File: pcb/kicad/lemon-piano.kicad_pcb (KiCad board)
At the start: 2 copper layers, 100 x 30 mm, 44 parts, among them J1 5V_IN, J2 LEMON_KEYS, SW1 SENS+, SW2 SENS-, U1 Nano_socket_A, U2 Nano_socket_B

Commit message: fix(pcb): v0.2.0 — real Nano orientation (erratum ADR-015) + full render suite
The photo-overlay verification caught v0.1.0's socket maps being
180°-rotated (TX1/VIN are at the ICSP end on real Nanos, D12/D13 at the
mini-USB end — verified on the official 2008 V2.2 board photo and
clones). v0.1.0 only worked inserted USB-east, where the buzzer blocks
the plug; its release folder is renamed v0.1.0-ERRATUM-do-not-fab.

v0.2.0 keeps the mechanics (USB corridor west) and fixes the maps:
keys header SOUTH (1..7 G under A0-A6), LED bar NORTH ascending
east→west, pull-ups with their pins; ground truth, schematic, netlist
and every gate re-derived — DRC 0/0/0, ERC 0/0, verify_placement/
holes/geometry PASS, fab zip under pcb/releases/v0.2.0/.

Render suite via the pcb-designer service v0.3.0 (3D models installed):
bare / dim / realistic / realistic-dim per side + photo overlay with a
real Nano image (Wikimedia Commons File:Arduino Nano.jpg, CC BY 2.0,
provenance in pcb/overlays/modules.yaml). post_route self-healing
upgrades (connectivity-based island bridging, split-net repair, exact
clearance geometry, IsOnLayer fix) in ADR-018.

Co-Authored-By: Claude Fable 5 <noreply@anthropic.com>
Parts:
- moved D3 49.6 mm to (145.3, 101.7), turned to -90 degrees
- moved D12 48.9 mm to (103.9, 101.7), turned to -90 degrees
- moved R8 48.2 mm to (147.6, 103.0)
- moved R17 47.5 mm to (106.2, 103.0)
- moved D4 42.1 mm to (140.7, 101.7), turned to -90 degrees
- moved D11 41.5 mm to (108.5, 101.7), turned to -90 degrees
- moved R9 40.5 mm to (143.0, 103.0)
- moved R16 39.9 mm to (110.8, 103.0)
- moved D5 35.5 mm to (136.1, 101.7), turned to -90 degrees
- moved D10 34.9 mm to (113.1, 101.7), turned to -90 degrees
- moved R10 33.6 mm to (138.4, 103.0)
- moved R15 33.0 mm to (115.4, 103.0)
- moved D6 30.2 mm to (131.5, 101.7), turned to -90 degrees
- moved D9 29.8 mm to (117.7, 101.7), turned to -90 degrees
- moved R11 27.9 mm to (133.8, 103.0)
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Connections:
- J2 pad 1: /GND -> /KEY1
- J2 pad 2: /KEY7 -> /KEY2
- J2 pad 3: /KEY6 -> /KEY3
- J2 pad 4: /KEY5 -> /KEY4
- J2 pad 5: /KEY4 -> /KEY5
- J2 pad 6: /KEY3 -> /KEY6
- J2 pad 7: /KEY2 -> /KEY7
- J2 pad 8: /KEY1 -> /GND
- R1 pad 1: /+5V -> /KEY1
- R1 pad 2: /KEY1 -> /+5V
- R18 pad 1: /+5V -> /SENS_MINUS
- R18 pad 2: /SENS_MINUS -> /+5V
- R2 pad 1: /+5V -> /KEY2
- R2 pad 2: /KEY2 -> /+5V
- R3 pad 1: /+5V -> /KEY3
- R3 pad 2: /KEY3 -> /+5V
- R4 pad 1: /+5V -> /KEY4
- R4 pad 2: /KEY4 -> /+5V
- R5 pad 1: /+5V -> /KEY5
- R5 pad 2: /KEY5 -> /+5V
- R6 pad 1: /+5V -> /KEY6
- R6 pad 2: /KEY6 -> /+5V
- R7 pad 1: /+5V -> /KEY7
- R7 pad 2: /KEY7 -> /+5V
- U1 pad 1: (no net) -> /BUZZER
- U1 pad 10: /LED6 -> /KEY7
- U1 pad 11: /LED7 -> /SENS_MINUS
- U1 pad 12: /LED8 -> /+5V
- U1 pad 13: /LED9 -> (no net)
- U1 pad 14: /LED10 -> /GND
- U1 pad 15: /SENS_PLUS -> (no net)
- U1 pad 4: /GND -> /KEY1
- U1 pad 5: /LED1 -> /KEY2
- U1 pad 6: /LED2 -> /KEY3
- U1 pad 7: /LED3 -> /KEY4
- U1 pad 8: /LED4 -> /KEY5
- U1 pad 9: /LED5 -> /KEY6
- U2 pad 1: /BUZZER -> (no net)
- U2 pad 10: /KEY7 -> /LED6
- U2 pad 11: /SENS_MINUS -> /LED7
- U2 pad 12: /+5V -> /LED8
- U2 pad 13: (no net) -> /LED9
- U2 pad 14: /GND -> /LED10
- U2 pad 15: (no net) -> /SENS_PLUS
- U2 pad 4: /KEY1 -> /GND
- U2 pad 5: /KEY2 -> /LED1
- U2 pad 6: /KEY3 -> /LED2
- U2 pad 7: /KEY4 -> /LED3
- U2 pad 8: /KEY5 -> /LED4
- U2 pad 9: /KEY6 -> /LED5
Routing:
- net /SENS_PLUS: track 17.0 -> 58.9 mm
- net /BUZZER: track 10.5 -> 47.5 mm, vias 0 -> 1
- net /SENS_MINUS: track 61.5 -> 40.6 mm, vias 1 -> 0
- net /GND: track 0.00 -> 14.8 mm, vias 0 -> 1
- net /LED3: track 7.84 -> 14.8 mm
- net /+5V: track 80.0 -> 86.0 mm
- net /LED1: track 12.0 -> 17.2 mm
- net /LED4: track 5.78 -> 11.0 mm
- net /LED2: track 9.90 -> 15.2 mm
- net /LED10: track 9.18 -> 4.28 mm
- net /LED5: track 4.14 -> 8.98 mm
- net /LED9: track 7.12 -> 3.43 mm
- net /LED6: track 3.29 -> 6.92 mm
- net /LED7_K: track 3.93 -> 2.43 mm
- net /LED1_K: track 3.93 -> 2.43 mm
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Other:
- board text added: "v0.2.0"
- board text removed: "v0.1.0"

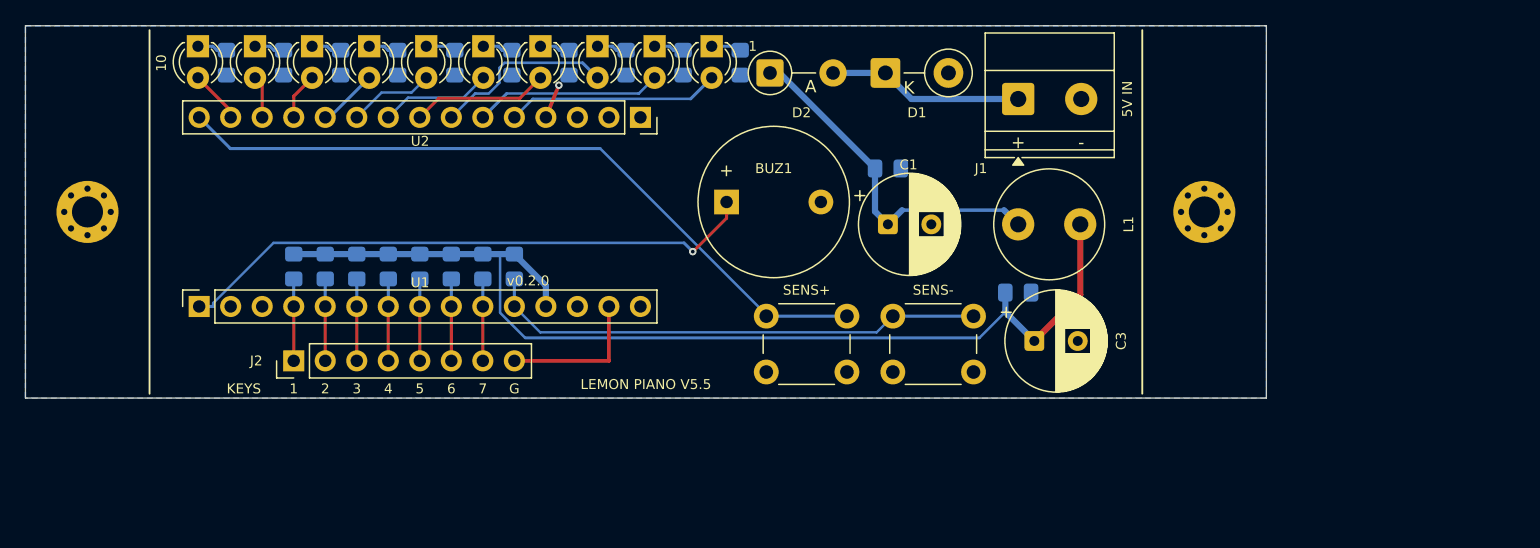
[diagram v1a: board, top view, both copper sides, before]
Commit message: feat(pcb): v0.2.1 — pin legends + full component labels + render suite naming
- 'pcb vX.Y.Z' version silk (front + back); MT1-style per-pin legends
  on both Nano socket rows; every component ref visible on its layer
  (bottom passives on B.SilkS; LED refs on the back — no front room at
  4.6 mm pitch). ADR-019.
- Render suite per version: renders/<ver>-{normal,dim,realistic,overlay}
  -{top,bottom}.png — realistic-dim dropped, overlay composites moved
  into renders/, overlays/ keeps only module photos + modules.yaml.
  v0.2.0 artefacts renamed/cleaned to the same scheme.
- Full gated pipeline re-run: DRC 0/0/0, ERC 0/0, verify_placement/
  holes/geometry PASS, fab zip releases/v0.2.1/.

Co-Authored-By: Claude Fable 5 <noreply@anthropic.com>
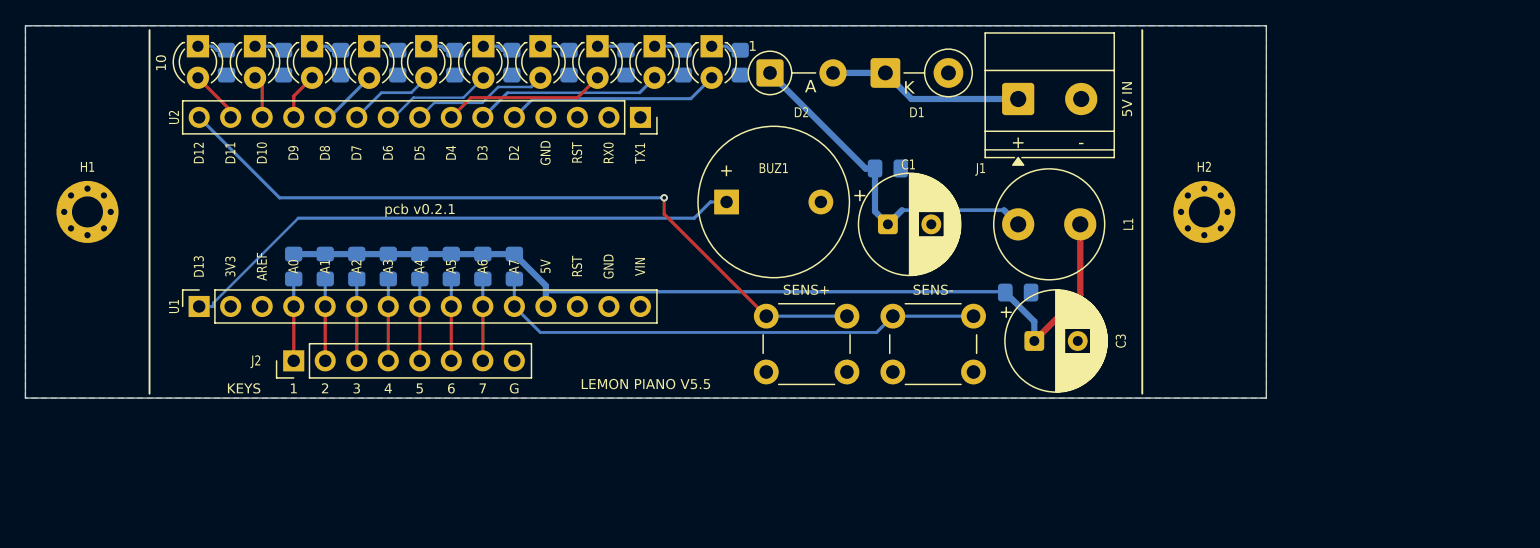
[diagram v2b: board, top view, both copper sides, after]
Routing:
- net /GND: track 14.8 -> 0.00 mm, vias 1 -> 0
- net /+5V: track 86.0 -> 75.9 mm
- net /LED3: track 14.8 -> 13.1 mm
- net /BUZZER: track 47.5 -> 46.2 mm, vias 1 -> 0
- net /SENS_PLUS: track 58.9 -> 59.6 mm, vias 0 -> 1
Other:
- board text added: "3V3"
- board text added: "5V"
- board text added: "A0"
- board text added: "A1"
- board text added: "A2"
- board text added: "A3"
- board text added: "A4"
- board text added: "A5"
- board text added: "A6"
- board text added: "A7"
- board text added: "AREF"
- board text added: "D10"
- board text added: "D11"
- board text added: "D12"
- board text added: "D13"
- board text added: "D2"
- board text added: "D3"
- board text added: "D4"
- board text added: "D5"
- board text added: "D6"
- board text added: "D7"
- board text added: "D8"
- board text added: "D9"
- board text added: "GND"
- board text added: "RST"
- board text added: "RX0"
- board text added: "TX1"
- board text added: "VIN"
- board text added: "pcb v0.2.1"
- board text removed: "v0.2.0"

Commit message: feat(pcb): v0.3.0 — 4 anchor holes, VU-meter LED colors, render fixes
- Two M2 anchors per short edge (x=95/185, y=105/125); hole-VISION
  verification enabled on transparent-bg renders (LL §22), LOO <=0.04 mm.
- LED1..10 = 3 green / 3 yellow / 2 orange / 2 red with per-LED colored
  3D bodies in the realistic renders (orange model shipped by the
  service). BOM values follow the colors.
- Realistic-bottom now shows all back-side parts (cloud /place no longer
  strips models from natively flipped footprints — toolkit fix e1320f5).
- Brighter Nano overlay photo (File:Arduino nano.jpg, CC BY-SA 4.0),
  recalibrated at 57.95 px/mm.
- post_route: split-net repair proven in anger (+5V chain), island
  healing can now chain through previously bridged islands.
- Full gated release: DRC 0/0/0, ERC 0/0, verify_placement/holes(+vision)/
  geometry PASS, fab zip releases/v0.3.0/. ADR-020..023.

Co-Authored-By: Claude Fable 5 <noreply@anthropic.com>
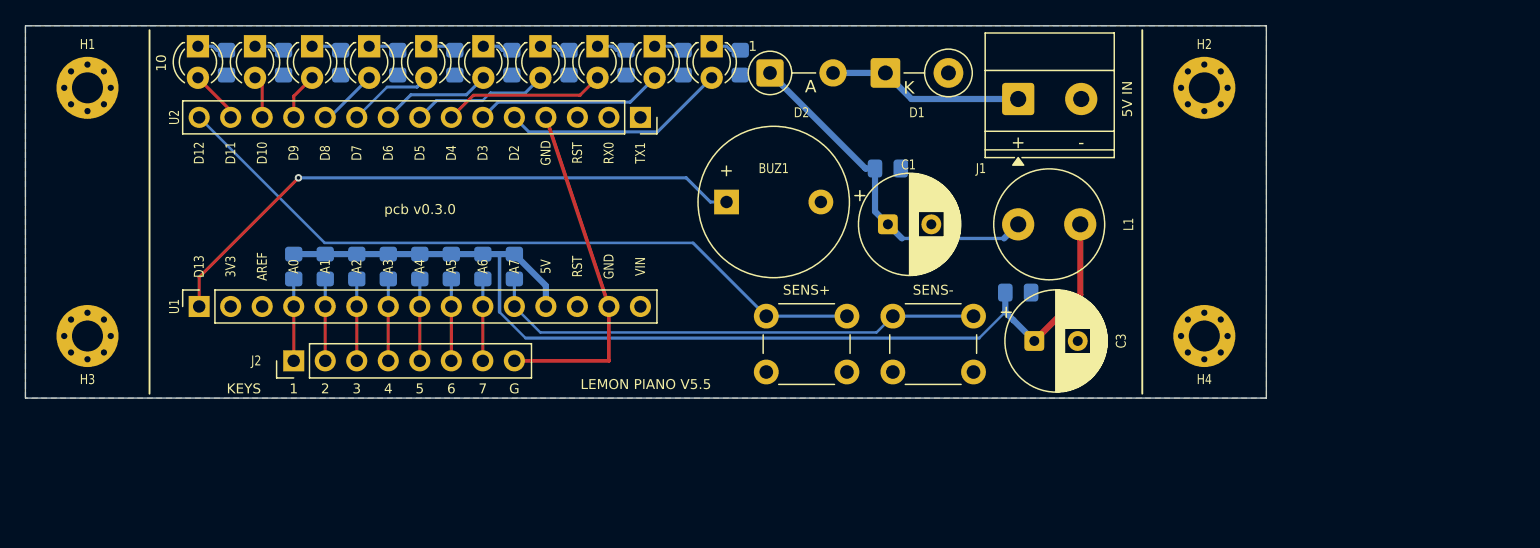
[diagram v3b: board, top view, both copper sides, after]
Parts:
- added H4: M2, MountingHole_2.5mm_Pad_Via, F.Cu at (185.0, 125.0)
- added J1: 5V_IN, TerminalBlock_Phoenix_MKDS-1,5-2-5.08_1x02_P5.08mm_Horizontal, F.Cu at (170.0, 105.9)
- D10: value GREEN_LED8 -> ORANGE
- D11: value GREEN_LED9 -> RED
- D12: value GREEN_LED10 -> RED
- D3: value GREEN_LED1 -> GREEN
- D4: value GREEN_LED2 -> GREEN
- D5: value GREEN_LED3 -> GREEN
- D6: value GREEN_LED4 -> YELLOW
- D7: value GREEN_LED5 -> YELLOW
- D8: value GREEN_LED6 -> YELLOW
- D9: value GREEN_LED7 -> ORANGE
- H3: renamed from J1; value 5V_IN -> M2; footprint TerminalBlock_Phoenix_MKDS-1,5-2-5.08_1x02_P5.08mm_Horizontal -> MountingHole_2.5mm_Pad_Via
- moved H3 77.4 mm to (95.0, 125.0)
- moved H1 10.0 mm to (95.0, 105.0)
- moved H2 10.0 mm to (185.0, 105.0)
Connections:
- H3 pad 1: /VIN -> /GND
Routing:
- net /GND: track 0.00 -> 28.1 mm
- net /+5V: track 75.9 -> 86.0 mm
- net /BUZZER: track 46.2 -> 49.0 mm, vias 0 -> 1
- net /LED1: track 17.2 -> 18.2 mm
- net /SENS_PLUS: track 59.6 -> 58.8 mm, vias 1 -> 0
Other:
- board text added: "pcb v0.3.0"
- board text removed: "pcb v0.2.1"

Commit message: feat(pcb): v0.4.0 — 120x40 remake, centred Nano, external-button headers
Complete floor-plan remake to the user's distribution spec. The V5.5
circuit is unchanged (no value, pin or part invented); only the board
frame and its interface changed.

- 120 x 40 mm frame (was 100 x 30), KiCad frame x 90..210 / y 100..140.
  Anchor dividers at x=100/200; four M2 holes to the corners at 5 mm
  insets (95/205 x 105/135), mirror-symmetric about x=150 and y=120.
- Nano socket centred on the board (pin field x 132.22..167.78, rows
  y 112.38/127.62), mini-USB still WEST. Centring it turned the USB
  corridor from a 14 mm sliver into a 42 mm strip, so the corridor is
  redefined as the band a cable needs (x < 130.4, y 113..127) and kept
  completely part-free, checked against real courtyard boxes.
- Whole 5 V filter in the west block, folded around that corridor: VIN
  section on the south strip (J1 -> D1 -> D2), VRAW/+5V on the north
  strip (C1 -> L1), output reservoir C3 at the south-strip east end.
  Three 8 mm radial parts do not fit one 27 mm strip, which forced the
  split. D2 at rot=180 so the chain reads west->east with no doubling
  back; EXPECTED_PADS locks that new rotation convention.
- 5 V entry is now a 2-pin 2.54 mm header (J1), replacing the Phoenix
  screw terminal, per the user's "2 pines". Same nets and polarity.
- A parallel 2-pin header per SENS button (J3 || SW1 on /SENS_PLUS,
  J4 || SW2 on /SENS_MINUS), each directly east of its button, so an
  external panel button plugs in without cutting a trace.
- Keys header centred on the south edge (pin centre exactly x=150);
  SENS button pair centred on y=120; LED bar centred over its D2..D11
  pin span so the fan legs stay short at both ends.
- Buzzer to the NE corner — the only place its 12.56 mm courtyard fits
  once the button column and EXT headers claim their x-lanes. Costs a
  ~58 mm /BUZZER run (piezo square wave over a solid plane: harmless).
- Title block moved into the USB corridor; KEYS word moved ea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
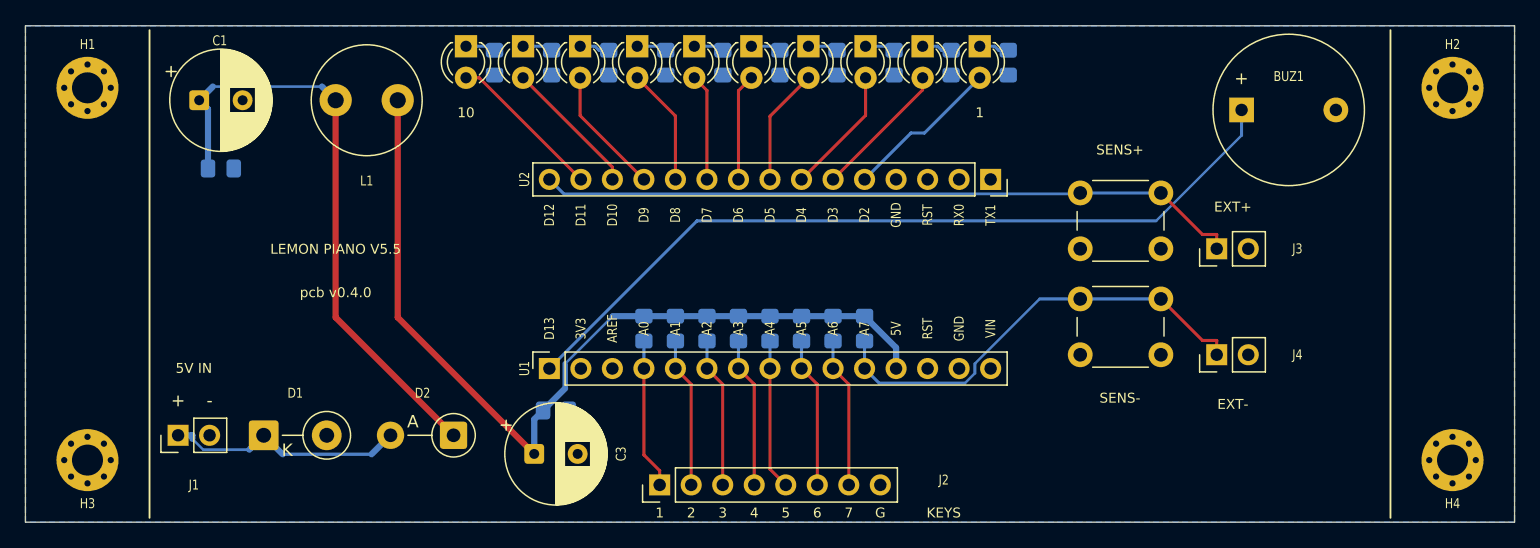
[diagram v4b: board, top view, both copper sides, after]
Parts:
- added J3: SENS+_EXT, PinHeader_1x02_P2.54mm_Vertical, F.Cu at (186.0, 118.0)
- added J4: SENS-_EXT, PinHeader_1x02_P2.54mm_Vertical, F.Cu at (186.0, 126.5)
- J1: footprint TerminalBlock_Phoenix_MKDS-1,5-2-5.08_1x02_P5.08mm_Horizontal -> PinHeader_1x02_P2.54mm_Vertical
- moved J1 72.9 mm to (102.3, 133.0), turned to 90 degrees
- moved D1 58.0 mm to (109.2, 133.0)
- moved C1 56.4 mm to (104.0, 106.0)
- moved L1 55.9 mm to (115.0, 106.0)
- moved C2 53.8 mm to (105.8, 111.5)
- moved BUZ1 42.2 mm to (188.0, 106.8)
- moved C3 41.3 mm to (131.0, 134.5)
- moved D2 38.8 mm to (124.5, 133.0), turned to 180 degrees
- moved C4 38.4 mm to (132.8, 131.0)
- moved J2 31.1 mm to (141.1, 137.0)
- moved R4 28.7 mm to (147.5, 124.4)
- moved R7 28.7 mm to (155.1, 124.4)
- moved R1 28.7 mm to (139.8, 124.4)
- moved R18 28.7 mm to (157.6, 124.4)
- moved R2 28.7 mm to (142.4, 124.4)
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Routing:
- net /GND: track 28.1 -> 0.00 mm
- net /VRAW: track 28.0 -> 48.6 mm
- net /BUZZER: track 49.0 -> 65.6 mm, vias 1 -> 0
- net /+5V: track 86.0 -> 72.3 mm
- net /LED10: track 4.28 -> 12.7 mm
- net /LED9: track 3.43 -> 11.2 mm
- net /LED8: track 3.80 -> 10.3 mm
- net /KEY6: track 6.60 -> 12.1 mm
- net /KEY3: track 6.60 -> 12.1 mm
- net /KEY2: track 6.60 -> 12.1 mm
- net /KEY1: track 6.60 -> 12.1 mm
- net /KEY5: track 6.60 -> 12.1 mm
- net /KEY7: track 6.60 -> 12.1 mm
- net /KEY4: track 6.60 -> 12.1 mm
- net /LED1: track 18.2 -> 12.7 mm
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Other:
- board size 100 x 30 mm -> 120 x 40 mm
- board text added: "EXT+"
- board text added: "EXT-"
- board text added: "pcb v0.4.0"
- board text removed: "pcb v0.3.0"
